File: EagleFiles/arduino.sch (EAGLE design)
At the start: 7 parts, among them IC1 ATMEGA328", IC2 74250N, IC3 74250N

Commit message: added another mux
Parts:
- added IC4: 74250N, 74xx-us:74250N
- added JP3: 1X16_HEADER", RBBB:1X16_HEADER"
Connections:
- new net N$41: IC1.(PCI18/INT0)PD2, IC4A.B
- new net N$42: IC1.(PCI16/RXD)PD0, IC4A.W
- new net N$43: IC1.(PCI20/XCK/T0)PD4, IC4A.D
- new net N$44: IC1.(PCI19/INT1/OC2B)PD3, IC4A.C
- new net N$45: IC1.(PCI17/TXD)PD1, IC4A.A
- new net N$46: IC4A.E15, JP3.1
- new net N$47: IC4A.E14, JP3.2
- new net N$48: IC4A.E13, JP3.3
- new net N$49: IC4A.E12, JP3.4
- new net N$50: IC4A.E11, JP3.5
- new net N$51: IC4A.E10, JP3.6
- new net N$52: IC4A.E9, JP3.7
- new net N$53: IC4A.E8, JP3.8
- new net N$54: IC4A.E7, JP3.9
- new net N$55: IC4A.E6, JP3.10
- new net N$56: IC4A.E5, JP3.11
- new net N$57: IC4A.E4, JP3.12
- new net N$58: IC4A.E3, JP3.13
- new net N$59: IC4A.E2, JP3.14
- new net N$60: IC4A.E1, JP3.15
- new net N$61: IC4A.E0, JP3.16
- net GND: now also IC1.PC6(/RESET/PCI14), IC4A.G
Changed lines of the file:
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@@
 <setting verticaltext="up"/>
 </settings>
-<grid distance="0.1" unitdist="inch" unit="inch" style="dots" multiple="1" display="yes" altdistance="0.01" altunitdist="inch" altunit="inch"/>
+<grid distance="0.1" unitdist="inch" unit="inch" style="lines" multiple="1" display="no" altdistance="0.01" altunitdist="inch" altunit="inch"/>
 <layers>
 <layer number="1" name="Top" color="4" fill="1" visible="no" active="no"/>
@@
 <part name="U$2" library="RBBB" deviceset="RESONATOR" device="&quot;"/>
 <part name="C1" library="capacitor-wima" deviceset="C" device="2,5-3" value="0.1 uF"/>
+<part name="IC4" library="74xx-us" deviceset="74*250" device="N"/>
+<part name="SUPPLY1" library="supply2" deviceset="GND" device=""/>
+<part name="JP3" library="RBBB" deviceset="1X16_HEADER" device="&quot;"/>
 </parts>
 <sheets>
@@
 <instance part="U$2" gate="G$1" x="27.94" y="78.74" rot="R270"/>
 <instance part="C1" gate="G$1" x="48.26" y="83.82"/>
+<instance part="IC4" gate="A" x="210.82" y="-78.74" rot="R180"/>
+<instance part="SUPPLY1" gate="GND" x="160.02" y="-48.26"/>
+<instance part="JP3" gate="G$1" x="243.84" y="-86.36" rot="R180"/>
 </instances>
 <busses>
@@
 <wire x1="20.32" y1="78.74" x2="20.32" y2="68.58" width="0.1524" layer="91"/>
 <wire x1="20.32" y1="68.58" x2="38.1" y2="68.58" width="0.1524" layer="91"/>
+<pinref part="IC1" gate="G$1" pin="PC6(/RESET/PCI14)"/>
+<wire x1="63.5" y1="99.06" x2="38.1" y2="99.06" width="0.1524" layer="91"/>
+<wire x1="38.1" y1="99.06" x2="38.1" y2="93.98" width="0.1524" layer="91"/>
+<junction x="38.1" y="93.98"/>
+</segment>
+<segment>
+<pinref part="IC4" gate="A" pin="G"/>
+<wire x1="223.52" y1="-50.8" x2="223.52" y2="-45.72" width="0.1524" layer="91"/>
+<pinref part="SUPPLY1" gate="GND" pin="GND"/>
+<wire x1="223.52" y1="-45.72" x2="160.02" y2="-45.72" width="0.1524" layer="91"/>
 </segment>
 </net>
@@
 </segment>
 </net>
+<net name="N$42" class="0">
+<segment>
+<pinref part="IC4" gate="A" pin="W"/>
+<wire x1="198.12" y1="-104.14" x2="149.86" y2="-104.14" width="0.1524" layer="91"/>
+<wire x1="149.86" y1="-104.14" x2="149.86" y2="73.66" width="0.1524" layer="91"/>
+<pinref part="IC1" gate="G$1" pin="(PCI16/RXD)PD0"/>
+<wire x1="149.86" y1="73.66" x2="119.38" y2="73.66" width="0.1524" layer="91"/>
+</segment>
+</net>
+<net name="N$43" class="0">
+<segment>
+<pinref part="IC4" gate="A" pin="D"/>
+<wire x1="223.52" y1="-53.34" x2="226.06" y2="-53.34" width="0.1524" layer="91"/>
+<wire x1="226.06" y1="-53.34" x2="226.06" y2="-43.18" width="0.1524" layer="91"/>
+<wire x1="226.06" y1="-43.18" x2="139.7" y2="-43.18" width="0.1524" layer="91"/>
+<wire x1="139.7" y1="-43.18" x2="139.7" y2="63.5" width="0.1524" layer="91"/>
+<pinref part="IC1" gate="G$1" pin="(PCI20/XCK/T0)PD4"/>
+<wire x1="139.7" y1="63.5" x2="119.38" y2="63.5" width="0.1524" layer="91"/>
+</segment>
+</net>
+<net name="N$44" class="0">
+<segment>
+<pinref part="IC4" gate="A" pin="C"/>
+<wire x1="223.52" y1="-55.88" x2="228.6" y2="-55.88" width="0.1524" layer="91"/>
+<wire x1="228.6" y1="-55.88" x2="228.6" y2="-40.64" width="0.1524" layer="91"/>
+<wire x1="228.6" y1="-40.64" x2="142.24" y2="-40.64" width="0.1524" layer="91"/>
+<wire x1="142.24" y1="-40.64" x2="142.24" y2="66.04" width="0.1524" layer="91"/>
+<pinref part="IC1" gate="G$1" pin="(PCI19/INT1/OC2B)PD3"/>
+<wire x1="142.24" y1="66.04" x2="119.38" y2="66.04" width="0.1524" layer="91"/>
+</segment>
+</net>
+<net name="N$41" class="0">
+<segment>
+<pinref part="IC4" gate="A" pin="B"/>
+<wire x1="223.52" y1="-58.42" x2="231.14" y2="-58.42" width="0.1524" layer="91"/>
+<wire x1="231.14" y1="-58.42" x2="231.14" y2="-38.1" width="0.1524" layer="91"/>
+<wire x1="231.14" y1="-38.1" x2="144.78" y2="-38.1" width="0.1524" layer="91"/>
+<wire x1="144.78" y1="-38.1" x2="144.78" y2="68.58" width="0.1524" layer="91"/>
+<pinref part="IC1" gate="G$1" pin="(PCI18/INT0)PD2"/>
+<wire x1="144.78" y1="68.58" x2="119.38" y2="68.58" width="0.1524" layer="91"/>
+</segment>
+</net>
+<net name="N$45" class="0">
+<segment>
+<pinref part="IC4" gate="A" pin="A"/>
+<wire x1="223.52" y1="-60.96" x2="233.68" y2="-60.96" width="0.1524" layer="91"/>
+<wire x1="233.68" y1="-60.96" x2="233.68" y2="-35.56" width="0.1524" layer="91"/>
+<wire x1="233.68" y1="-35.56" x2="147.32" y2="-35.56" width="0.1524" layer="91"/>
+<wire x1="147.32" y1="-35.56" x2="147.32" y2="71.12" width="0.1524" layer="91"/>
+<pinref part="IC1" gate="G$1" pin="(PCI17/TXD)PD1"/>
+<wire x1="147.32" y1="71.12" x2="119.38" y2="71.12" width="0.1524" layer="91"/>
+</segment>
+</net>
+<net name="N$46" class="0">
+<segment>
+<pinref part="JP3" gate="G$1" pin="1"/>
+<pinref part="IC4" gate="A" pin="E15"/>
+<wire x1="233.68" y1="-66.04" x2="223.52" y2="-66.04" width="0.1524" layer="91"/>
+</segment>
+</net>
+<net name="N$47" class="0">
+<segment>
+<pinref part="IC4" gate="A" pin="E14"/>
+<pinref part="JP3" gate="G$1" pin="2"/>
+<wire x1="223.52" y1="-68.58" x2="233.68" y2="-68.58" width="0.1524" layer="91"/>
+</segment>
+</net>
+<net name="N$48" class="0">
+<segment>
+<pinref part="JP3" gate="G$1" pin="3"/>
+<pinref part="IC4" gate="A" pin="E13"/>
+<wire x1="233.68" y1="-71.12" x2="223.52" y2="-71.12" width="0.1524" layer="91"/>
+</segment>
+</net>
+<net name="N$49" class="0">
+<segment>
+<pinref part="IC4" gate="A" pin="E12"/>
+<pinref part="JP3" gate="G$1" pin="4"/>
+<wire x1="223.52" y1="-73.66" x2="233.68" y2="-73.66" width="0.1524" layer="91"/>
+</segment>
+</net>
+<net name="N$50" class="0">
+<segment>
+<pinref part="JP3" gate="G$1" pin="5"/>
+<pinref part="IC4" gate="A" pin="E11"/>
+<wire x1="233.68" y1="-76.2" x2="223.52" y2="-76.2" width="0.1524" layer="91"/>
+</segment>
+</net>
+<net name="N$51" class="0">
+<segment>
+<pinref part="IC4" gate="A" pin="E10"/>
+<pinref part="JP3" gate="G$1" pin="6"/>
+<wire x1="223.52" y1="-78.74" x2="233.68" y2="-78.74" width="0.1524" layer="91"/>
+</segment>
+</net>
+<net name="N$52" class="0">
+<segment>
+<pinref part="JP3" gate="G$1" pin="7"/>
+<pinref part="IC4" gate="A" pin="E9"/>
+<wire x1="233.68" y1="-81.28" x2="223.52" y2="-81.28" width="0.1524" layer="91"/>
+</segment>
+</net>
+<net name="N$53" class="0">
+<segment>
+<pinref part="IC4" gate="A" pin="E8"/>
+<pinref part="JP3" gate="G$1" pin="8"/>
+<wire x1="223.52" y1="-83.82" x2="233.68" y2="-83.82" width="0.1524" layer="91"/>
+</segment>
+</net>
+<net name="N$54" class="0">
+<segment>
+<pinref part="JP3" gate="G$1" pin="9"/>
+<pinref part="IC4" gate="A" pin="E7"/>
+<wire x1="233.68" y1="-86.36" x2="223.52" y2="-86.36" width="0.1524" layer="91"/>
+</segment>
+</net>
+<net name="N$55" class="0">
+<segment>
+<pinref part="IC4" gate="A" pin="E6"/>
+<pinref part="JP3" gate="G$1" pin="10"/>
+<wire x1="223.52" y1="-88.9" x2="233.68" y2="-88.9" width="0.1524" layer="91"/>
+</segment>
+</net>
+<net name="N$56" class="0">
+<segment>
+<pinref part="JP3" gate="G$1" pin="11"/>
+<pinref part="IC4" gate="A" pin="E5"/>
+<wire x1="233.68" y1="-91.44" x2="223.52" y2="-91.44" width="0.1524" layer="91"/>
+</segment>
+</net>
+<net name="N$57" class="0">
+<segment>
+<pinref part="IC4" gate="A" pin="E4"/>
+<pinref part="JP3" gate="G$1" pin="12"/>
+<wire x1="223.52" y1="-93.98" x2="233.68" y2="-93.98" width="0.1524" layer="91"/>
+</segment>
+</net>
+<net name="N$58" class="0">
+<segment>
+<pinref part="JP3" gate="G$1" pin="13"/>
+<pinref part="IC4" gate="A" pin="E3"/>
+<wire x1="233.68" y1="-96.52" x2="223.52" y2="-96.52" width="0.1524" layer="91"/>
+</segment>
+</net>
+<net name="N$59" class="0">
+<segment>
+<pinref part="IC4" gate="A" pin="E2"/>
+<pinref part="JP3" gate="G$1" pin="14"/>
+<wire x1="223.52" y1="-99.06" x2="233.68" y2="-99.06" width="0.1524" layer="91"/>
+</segment>
+</net>
+<net name="N$60" class="0">
+<segment>
+<pinref part="JP3" gate="G$1" pin="15"/>
+<pinref part="IC4" gate="A" pin="E1"/>
+<wire x1="233.68" y1="-101.6" x2="223.52" y2="-101.6" width="0.1524" layer="91"/>
+</segment>
+</net>
+<net name="N$61" class="0">
+<segment>
+<pinref part="IC4" gate="A" pin="E0"/>
+<pinref part="JP3" gate="G$1" pin="16"/>
+<wire x1="223.52" y1="-104.14" x2="233.68" y2="-104.14" width="0.1524" layer="91"/>
+</segment>
+</net>

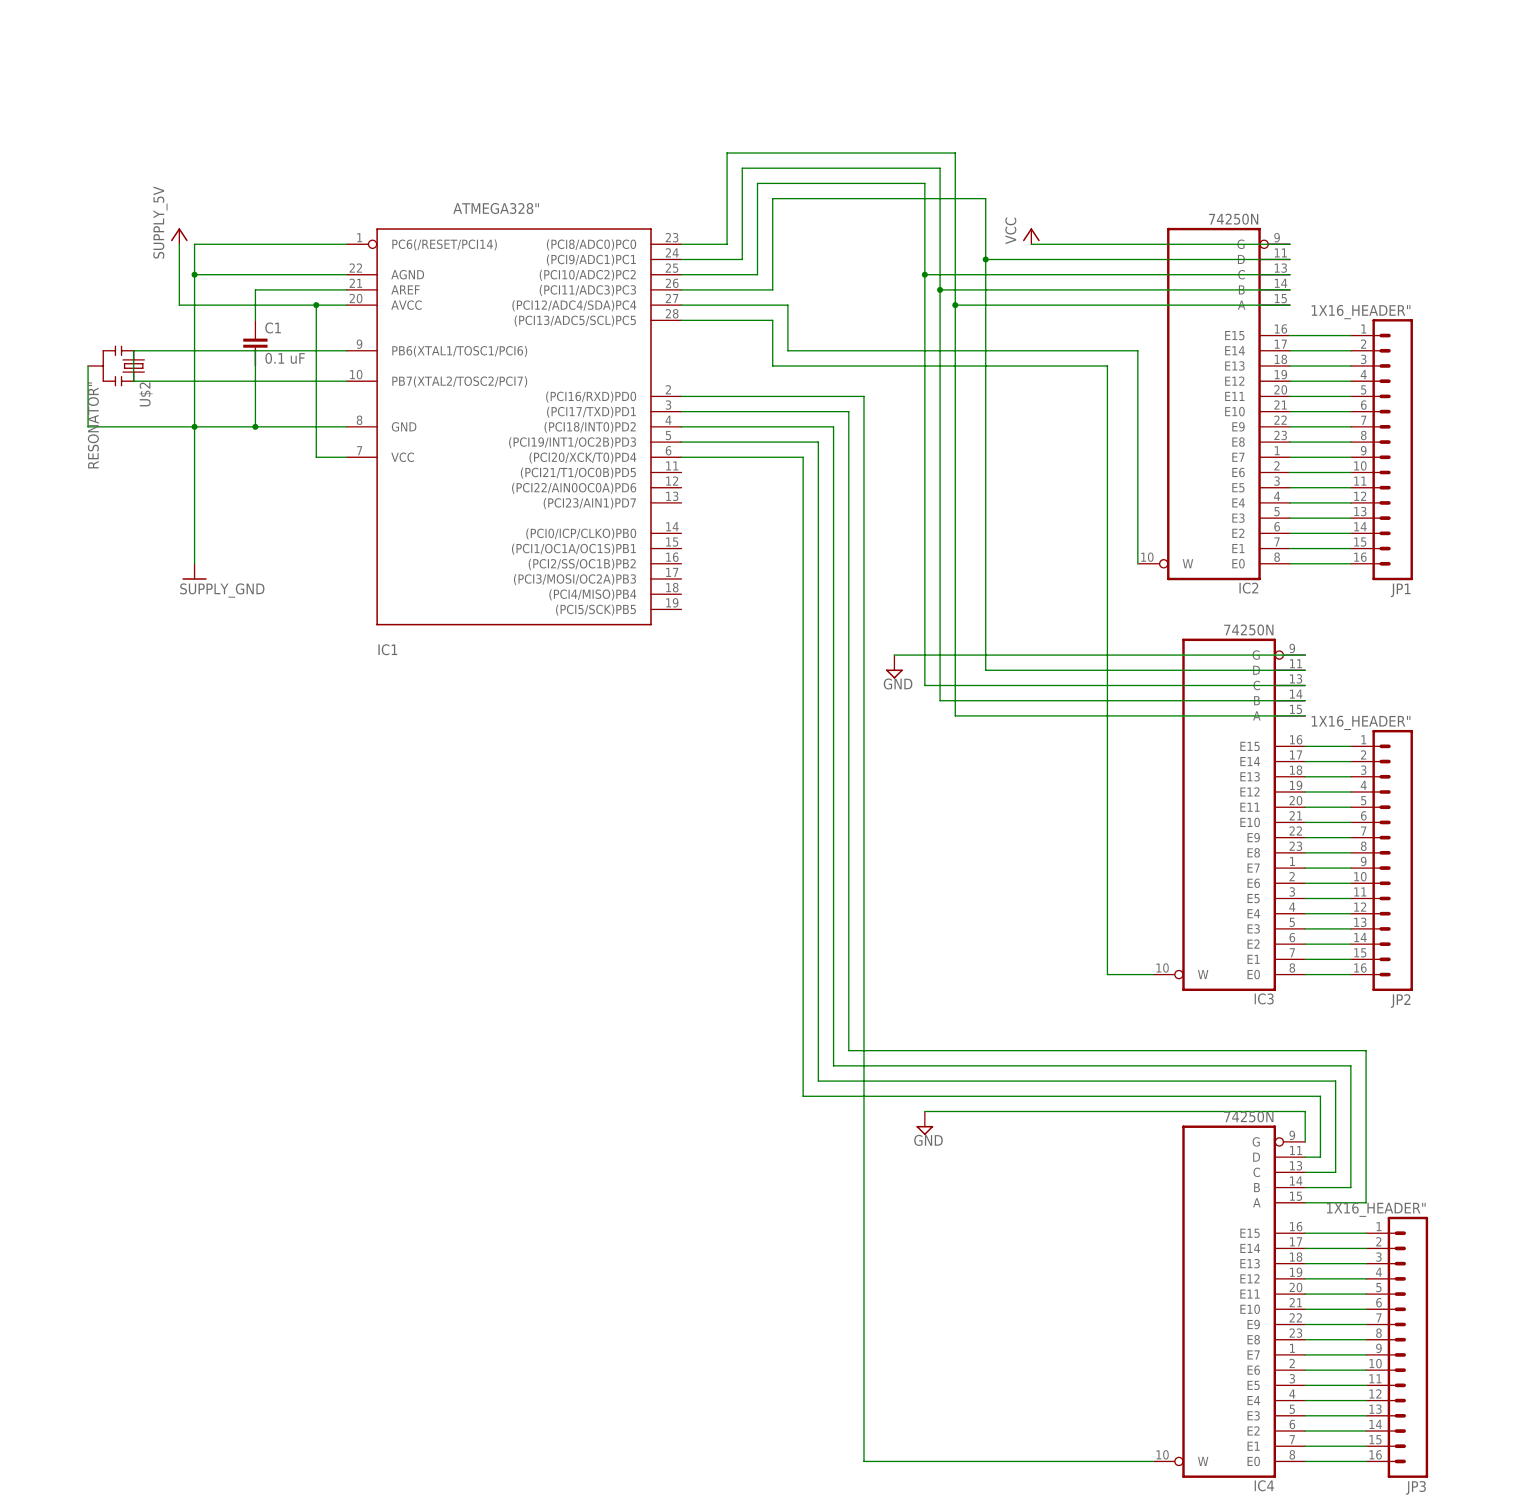
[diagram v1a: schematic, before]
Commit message: added most of the ic's
TODO:
    - power
    - hook up mux's right
    - verification
    - board
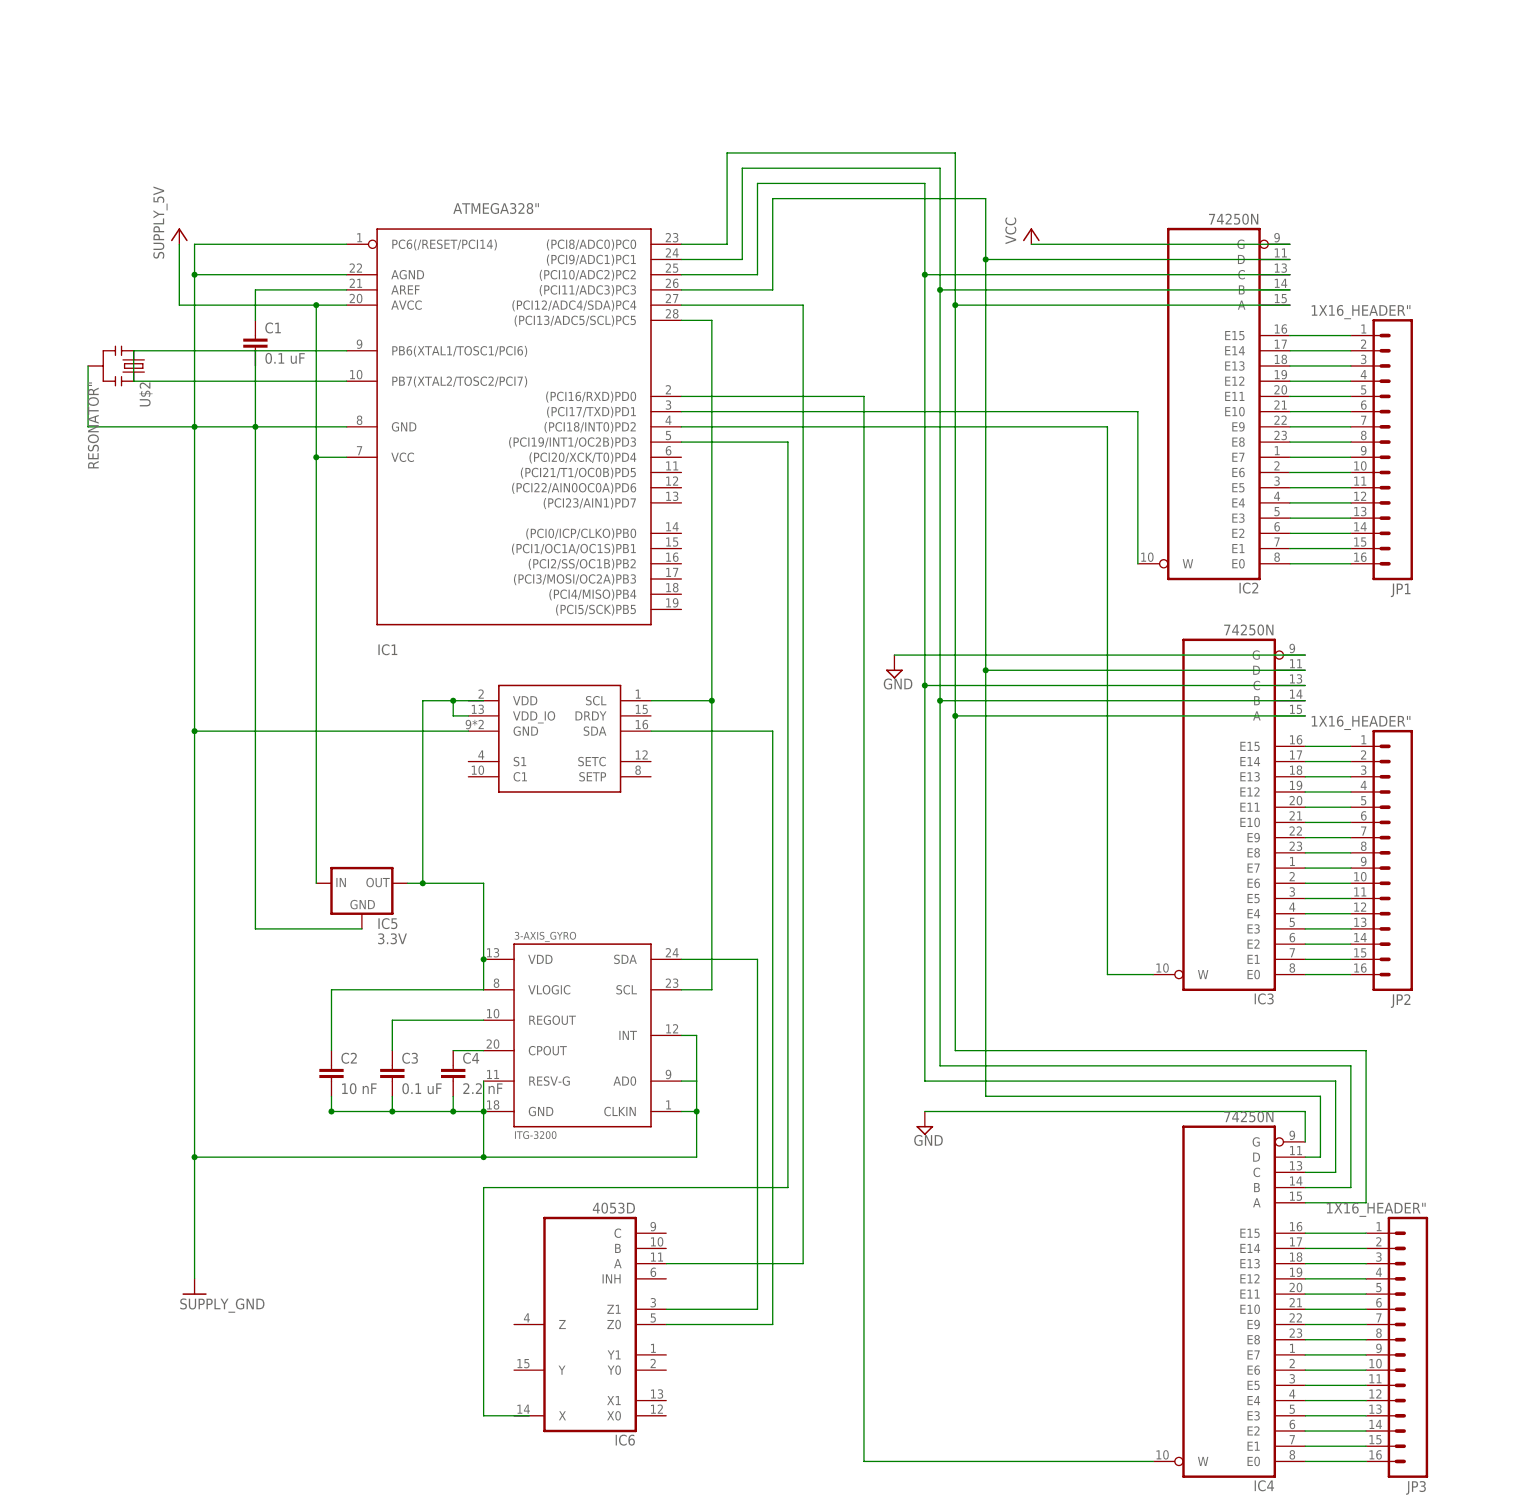
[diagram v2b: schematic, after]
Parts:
- added 3-AXIS_GYRO: ITG-3200, SparkFun:ITG-3200
- added 3-AXIS_MAG: HMC5883L, HMC5883L:HMC5883L
- added C2: 10 nF, SparkFun:CAPPTH
- added C3: 0.1 uF, SparkFun:CAPPTH
- added C4: 2.2 nF, SparkFun:CAPPTH
- added IC5: 3.3V, RBBB:REGULATOR
- added IC6: 4053D, 40xx:4053D
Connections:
- new net N$62: 3-AXIS_GYRO.SCL, 3-AXIS_MAG.SCL, IC1.(PCI13/ADC5/SCL)PC5
- new net N$64: 3-AXIS_GYRO.CPOUT, C4.1
- new net N$65: 3-AXIS_GYRO.REGOUT, C3.1
- new net N$67: 3-AXIS_GYRO.VDD, 3-AXIS_GYRO.VLOGIC, 3-AXIS_MAG.VDD_IO, C2.1, IC5.OUT
- net +5V: now also IC5.IN
- net GND: now also 3-AXIS_GYRO.AD0, 3-AXIS_GYRO.CLKIN, 3-AXIS_GYRO.GND, 3-AXIS_GYRO.INT, 3-AXIS_GYRO.RESV-G, 3-AXIS_MAG.GND, C2.2, C3.2, C4.2, IC5.GND
- net N$2: now also IC4A.C
- net N$3: now also IC4A.B
- net N$4: now also IC4A.A
- net N$41: now also IC1.(PCI12/ADC4/SDA)PC4, IC6A.A; no longer IC1.(PCI18/INT0)PD2, IC4A.B
- net N$43: now also IC1.(PCI19/INT1/OC2B)PD3; no longer IC1.(PCI20/XCK/T0)PD4, IC4A.D
- net N$44: now also 3-AXIS_MAG.SDA, IC6A.Z0; no longer IC1.(PCI19/INT1/OC2B)PD3, IC4A.C
- net N$45: now also 3-AXIS_GYRO.SDA, IC6A.Z1; no longer IC1.(PCI17/TXD)PD1, IC4A.A
- net N$5: now also IC1.(PCI17/TXD)PD1; no longer IC1.(PCI12/ADC4/SDA)PC4
- net N$6: now also IC1.(PCI18/INT0)PD2; no longer IC1.(PCI13/ADC5/SCL)PC5
- net N$7: now also IC4A.D
